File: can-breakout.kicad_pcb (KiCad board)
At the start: 2 copper layers, 30.5 x 10.2 mm, 10 parts, among them J1 Conn_01x04, J2 Conn_01x02, U1 SN65HVD230

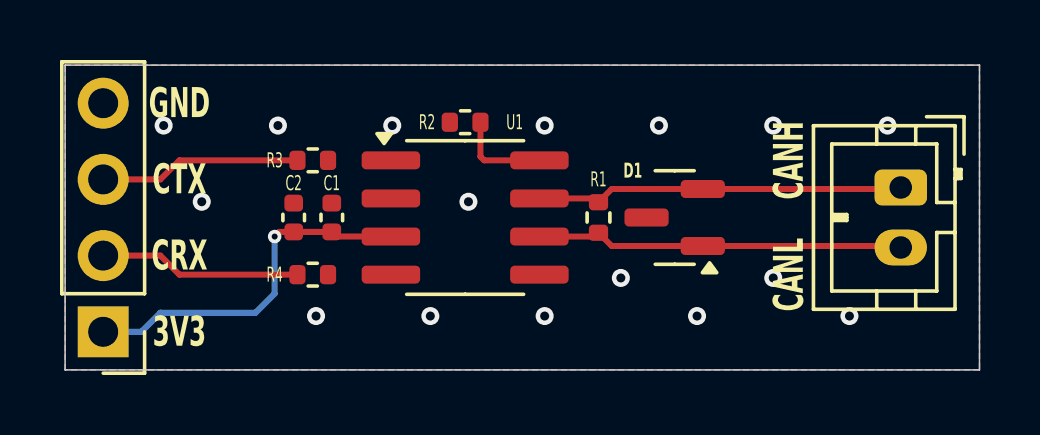
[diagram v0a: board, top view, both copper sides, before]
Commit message: fix: connecting current limiting resitors to sn65
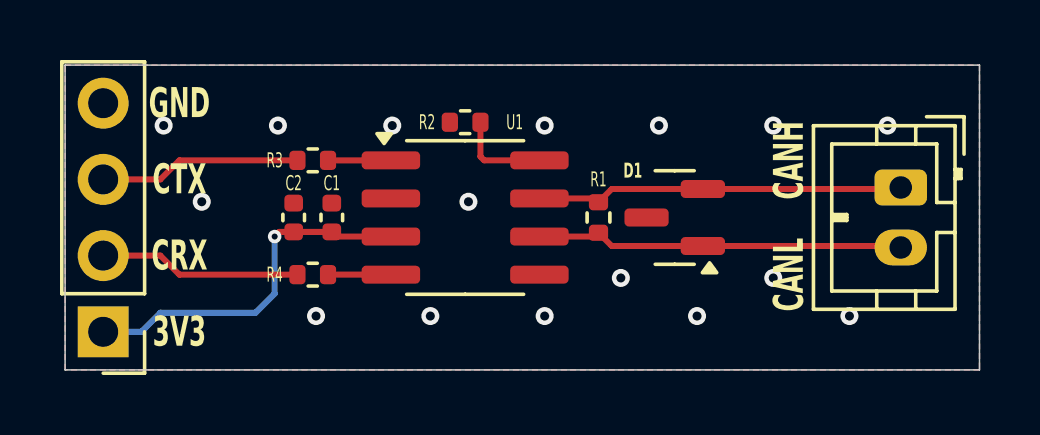
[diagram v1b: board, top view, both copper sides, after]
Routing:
- net Net-(U1-R): track 0.00 -> 2.09 mm
- net Net-(U1-D): track 0.00 -> 2.09 mm
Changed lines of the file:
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@@
+	)
+	(segment
+		(start 150.56 84.455)
+		(end 148.465 84.455)
+		(width 0.2032)
+		(layer "F.Cu")
+		(net 4)
+	)
+	(segment
+		(start 148.465 88.265)
+		(end 150.56 88.265)
+		(width 0.2032)
+		(layer "F.Cu")
+		(net 5)
 	)
 	(segment
